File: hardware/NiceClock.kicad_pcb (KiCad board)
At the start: 2 copper layers, 249 x 249 mm, 176 parts, among them P1 CONN_01X04, U1 WS2803, U10 MCP7940M, U2 WS2803, U3 WS2803, U4 WS2803, U5 WS2803, U6 WS2803, U7 WS2803, U8 STM32F101C8, U9 LM317EMP, Y1 8MHz, Y2 32.768kHz

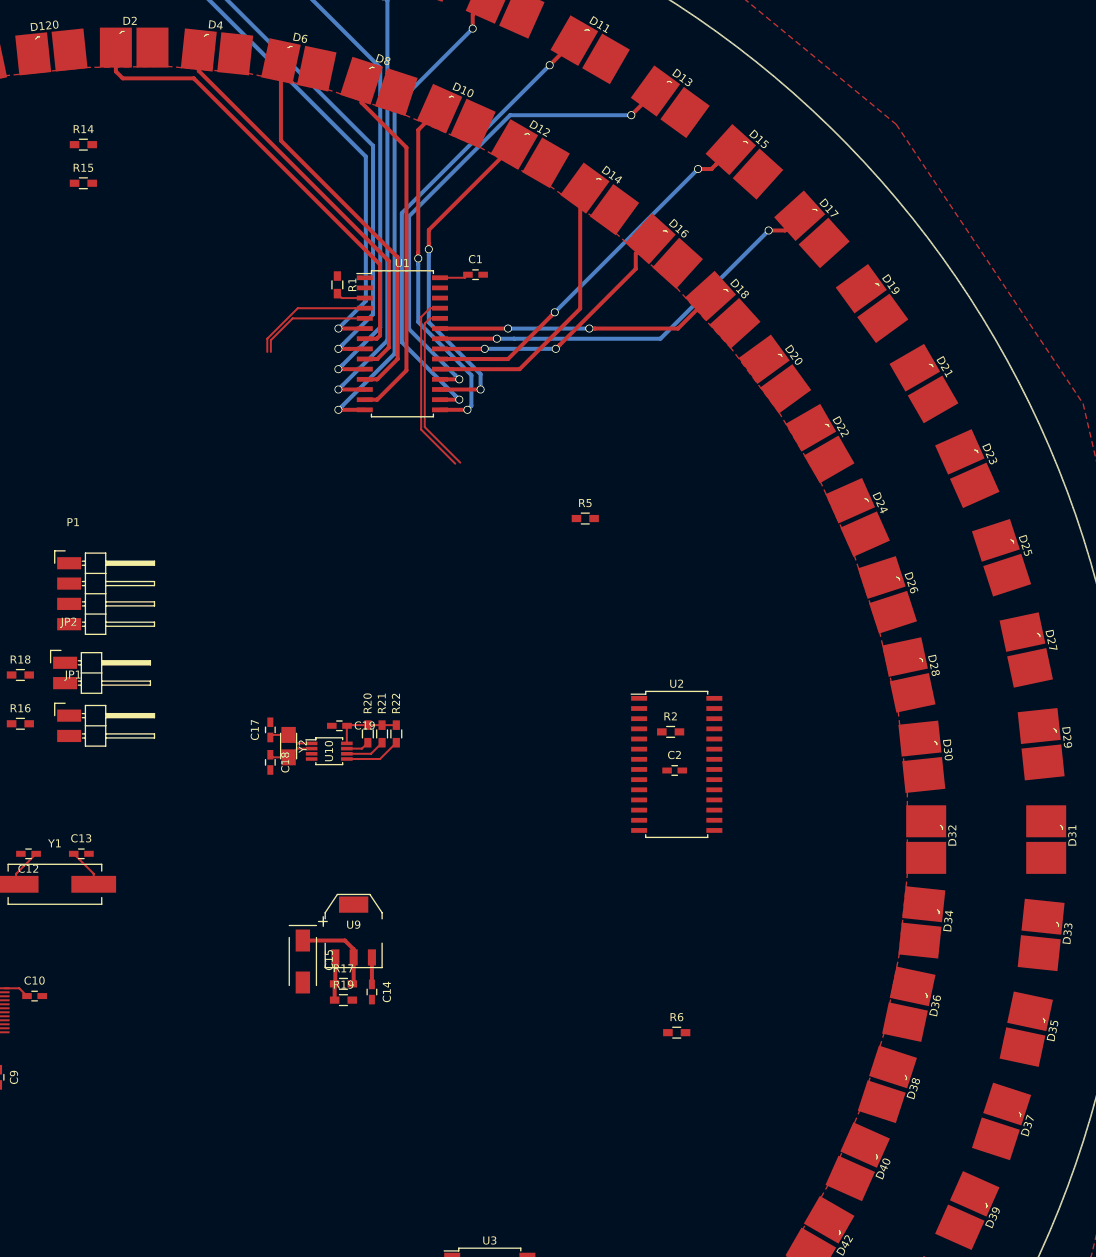
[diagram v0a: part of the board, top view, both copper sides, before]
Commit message: added switches, DC jack + some routing
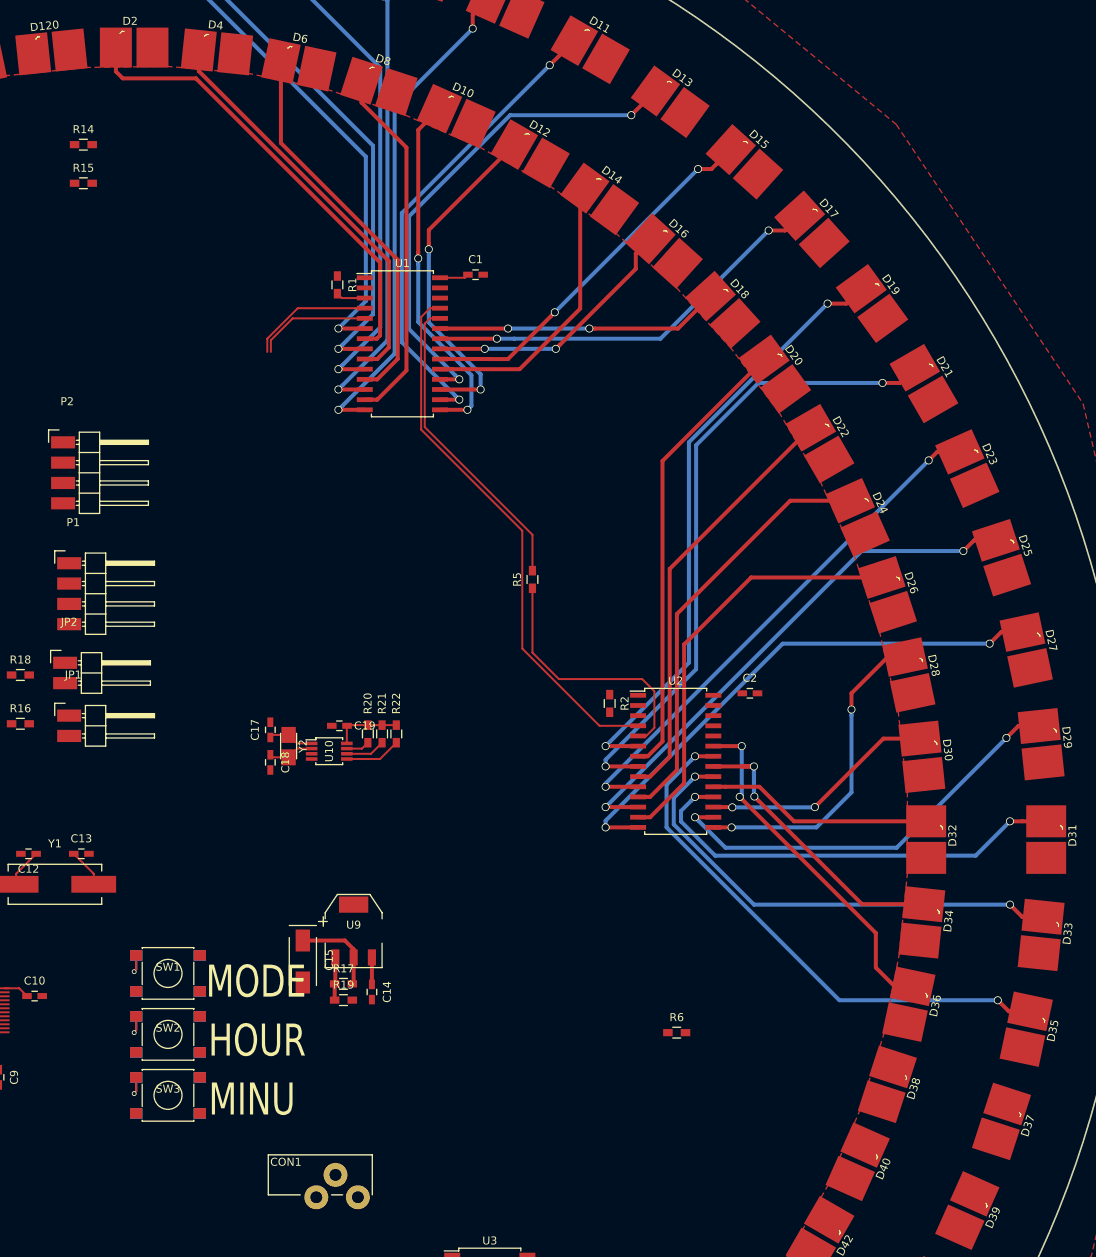
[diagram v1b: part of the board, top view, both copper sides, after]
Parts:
- added CON1: BARREL_JACK, custom_janh:DC_JACK1, F.Cu at (173.0, 189.2)
- added P2: CONN_01X04, custom_janh:Pin_Header_SMD_Angled_1x04, F.Cu at (147.8, 97.7)
- added SW1: SW_PUSH, Buttons_Switches_SMD:SW_SPST_PTS645, F.Cu at (160.4, 164.0)
- added SW2: SW_PUSH, Buttons_Switches_SMD:SW_SPST_PTS645, F.Cu at (160.4, 171.7)
- added SW3: SW_PUSH, Buttons_Switches_SMD:SW_SPST_PTS645, F.Cu at (160.4, 179.3)
- added SW4: SW_PUSH, Buttons_Switches_SMD:SW_SPST_PTS645, B.Cu at (160.4, 179.3)
- added SW5: SW_PUSH, Buttons_Switches_SMD:SW_SPST_PTS645, B.Cu at (160.4, 171.7)
- added SW6: SW_PUSH, Buttons_Switches_SMD:SW_SPST_PTS645, B.Cu at (160.4, 164.0)
- moved C2 13.5 mm to (233.2, 129.0)
- moved R5 10.1 mm to (206.0, 114.8), turned to 90 degrees
- moved R2 8.41 mm to (215.6, 130.3), turned to 270 degrees
- moved U2 0.40 mm to (223.9, 137.5)
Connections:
- U8 pad 26: Net-(U8-Pad26) -> /SW_M
- U8 pad 27: Net-(U8-Pad27) -> /SW_H
- U8 pad 28: Net-(U8-Pad28) -> /SW_MODE
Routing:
- net Net-(D21-Pad1): track 0.00 -> 80.2 mm, vias 0 -> 2
- net Net-(D19-Pad1): track 0.00 -> 75.9 mm, vias 0 -> 2
- net Net-(D35-Pad1): track 0.00 -> 67.6 mm, vias 0 -> 2
- net Net-(D27-Pad1): track 0.00 -> 66.8 mm, vias 0 -> 2
- net Net-(D25-Pad1): track 0.00 -> 66.7 mm, vias 0 -> 2
- net Net-(D23-Pad1): track 0.00 -> 65.9 mm, vias 0 -> 2
- net Net-(D33-Pad1): track 0.00 -> 60.3 mm, vias 0 -> 2
- net Net-(D20-Pad1): track 0.00 -> 56.9 mm
- net Net-(D31-Pad1): track 0.00 -> 55.3 mm, vias 0 -> 2
- net Net-(D22-Pad1): track 0.00 -> 53.4 mm
- net Net-(D24-Pad1): track 0.00 -> 53.3 mm
- net Net-(D29-Pad1): track 0.00 -> 53.2 mm, vias 0 -> 2
- net Net-(D26-Pad1): track 0.00 -> 53.0 mm
- net Net-(U1-Pad25): track 22.9 -> 68.0 mm
- net Net-(D36-Pad1): track 0.00 -> 44.0 mm, vias 0 -> 2
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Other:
- board text added: "HOUR"
- board text added: "MINU"
- board text added: "MODE"

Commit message: some updates
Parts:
- moved R7 31.9 mm to (199.1, 213.4)
- moved C4 30.4 mm to (161.5, 211.1)
- moved C3 29.2 mm to (220.4, 181.6)
- moved R3 25.0 mm to (203.2, 183.1), turned to 270 degrees
- moved U4 20.7 mm to (152.0, 219.6)
- moved U3 20.4 mm to (211.3, 190.1)
- moved R5 14.1 mm to (219.7, 118.1)
- moved R4 12.0 mm to (143.8, 212.1), turned to 270 degrees
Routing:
- net Net-(D53-Pad1): track 0.00 -> 72.0 mm, vias 0 -> 2
- net Net-(D37-Pad1): track 0.00 -> 70.6 mm, vias 0 -> 2
- net Net-(D55-Pad1): track 0.00 -> 70.5 mm, vias 0 -> 2
- net Net-(D39-Pad1): track 0.00 -> 63.3 mm, vias 0 -> 2
- net Net-(D41-Pad1): track 0.00 -> 61.8 mm, vias 0 -> 2
- net Net-(D57-Pad1): track 0.00 -> 60.6 mm, vias 0 -> 2
- net Net-(D51-Pad1): track 0.00 -> 59.7 mm, vias 0 -> 2
- net Net-(D45-Pad1): track 0.00 -> 59.6 mm, vias 0 -> 2
- net Net-(D43-Pad1): track 0.00 -> 57.4 mm, vias 0 -> 2
- net Net-(D54-Pad1): track 0.00 -> 57.0 mm
- net Net-(D40-Pad1): track 0.00 -> 56.2 mm, vias 0 -> 2
- net Net-(D59-Pad1): track 0.00 -> 56.0 mm, vias 0 -> 2
- net Net-(D38-Pad1): track 0.00 -> 51.5 mm
- net Net-(D49-Pad1): track 0.00 -> 48.7 mm, vias 0 -> 2
- net Net-(D42-Pad1): track 0.00 -> 46.5 mm, vias 0 -> 2
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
